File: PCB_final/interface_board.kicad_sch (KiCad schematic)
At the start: 106 parts, among them J1 02x30_Shift_Register_Connector, J2 02x30_ADC_Connector, U1 74HC595, U2 74HC595, U3 74HC595, U4 74HC595, U5 74HC595, U6 74HC595, U7 74HC595, U8 MAX11643EEG, U9 MAX11643EEG

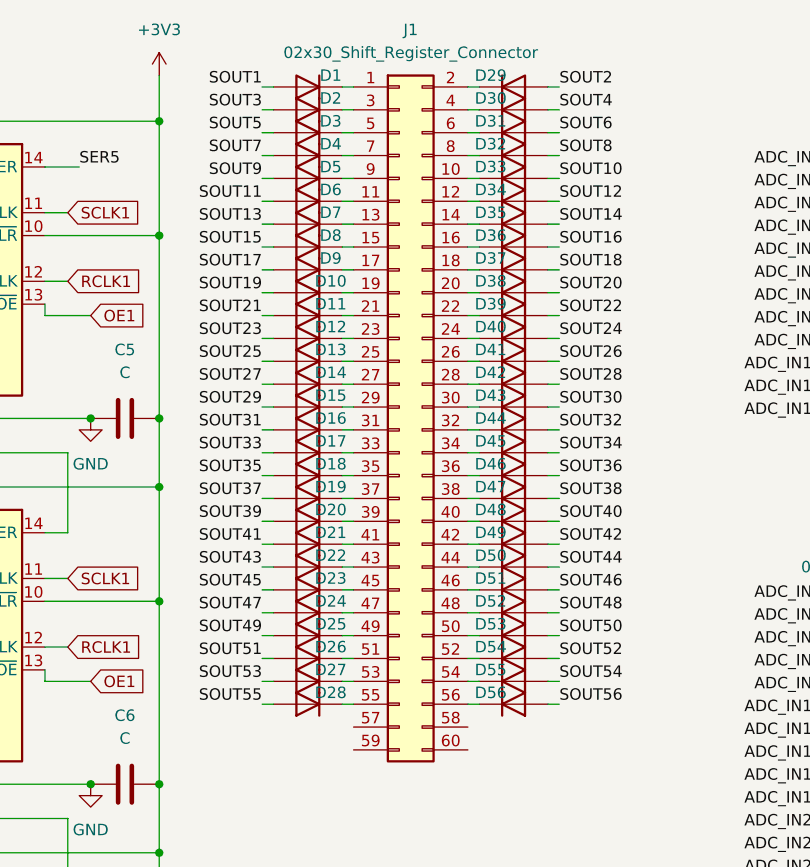
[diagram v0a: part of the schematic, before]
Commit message: changed diodes to the correct surface mount diodes we will be using on the final pcb
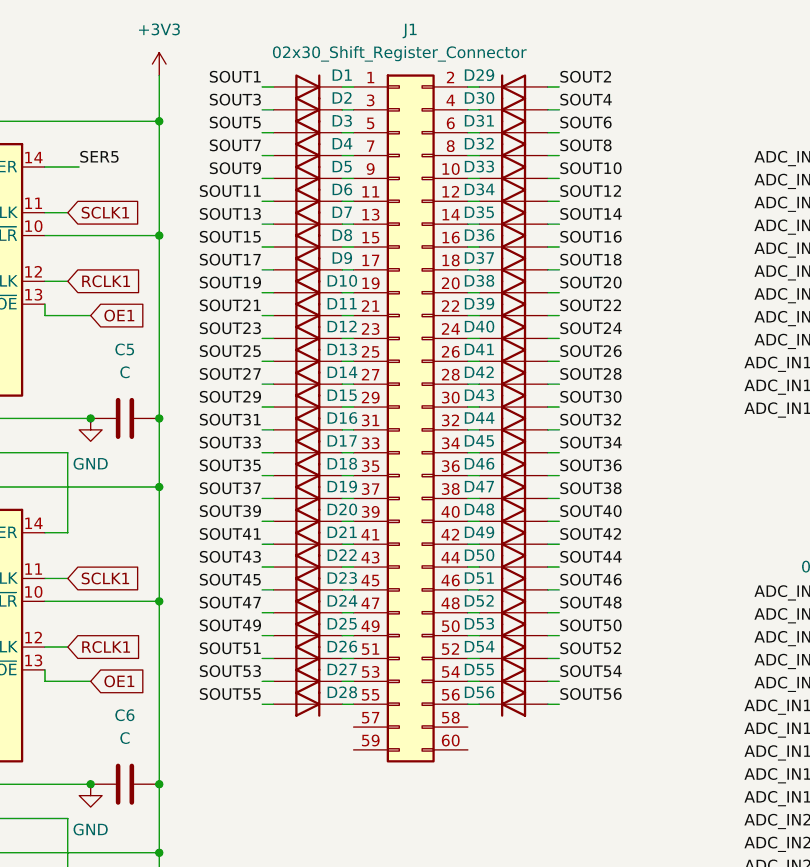
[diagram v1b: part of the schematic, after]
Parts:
- removed D1, D10, D11, D12, D13, D14, D15, D16, D17, D18, D19, D2, D20, D21, D22, D23, D24, D25, D26, D27, D28, D29, D3, D30, D31, D32, D33, D34, D35, D36, D37, D38, D39, D4, D40, D41, D42, D43, D44, D45, D46, D47, D48, D49, D5, D50, D51, D52, D53, D54, D55, D56, D6, D7, D8, D9: D, symbol Device:D
- added D1, D10, D11, D12, D13, D14, D15, D16, D17, D18, D19, D2, D20, D21, D22, D23, D24, D25, D26, D27, D28, D29, D3, D30, D31, D32, D33, D34, D35, D36, D37, D38, D39, D4, D40, D41, D42, D43, D44, D45, D46, D47, D48, D49, D5, D50, D51, D52, D53, D54, D55, D56, D6, D7, D8, D9: MMSD4148, Diode_SMD:D_SOD-123, symbol Diode:MMSD4148
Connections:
- net SOUT1: now also D1.2 (A)
- net SOUT10: now also D33.2 (A)
- net SOUT11: now also D6.2 (A)
- net SOUT12: now also D34.2 (A)
- net SOUT13: now also D7.2 (A)
- net SOUT14: now also D35.2 (A)
- net SOUT15: now also D8.2 (A)
- net SOUT16: now also D36.2 (A)
- net SOUT17: now also D9.2 (A)
- net SOUT18: now also D37.2 (A)
- net SOUT19: now also D10.2 (A)
- net SOUT2: now also D29.2 (A)
- net SOUT20: now also D38.2 (A)
- net SOUT21: now also D11.2 (A)
- net SOUT22: now also D39.2 (A)
- net SOUT23: now also D12.2 (A)
- net SOUT24: now also D40.2 (A)
- net SOUT25: now also D13.2 (A)
- net SOUT26: now also D41.2 (A)
- net SOUT27: now also D14.2 (A)
- net SOUT28: now also D42.2 (A)
- net SOUT29: now also D15.2 (A)
- net SOUT3: now also D2.2 (A)
- net SOUT30: now also D43.2 (A)
- net SOUT31: now also D16.2 (A)
- net SOUT32: now also D44.2 (A)
- net SOUT33: now also D17.2 (A)
- net SOUT34: now also D45.2 (A)
- net SOUT35: now also D18.2 (A)
- net SOUT36: now also D46.2 (A)
- net SOUT37: now also D19.2 (A)
- net SOUT38: now also D47.2 (A)
- net SOUT39: now also D20.2 (A)
- net SOUT4: now also D30.2 (A)
- net SOUT40: now also D48.2 (A)
- net SOUT41: now also D21.2 (A)
- net SOUT42: now also D49.2 (A)
- net SOUT43: now also D22.2 (A)
- net SOUT44: now also D50.2 (A)
- net SOUT45: now also D23.2 (A)
- net SOUT46: now also D51.2 (A)
- net SOUT47: now also D24.2 (A)
- net SOUT48: now also D52.2 (A)
- net SOUT49: now also D25.2 (A)
- net SOUT5: now also D3.2 (A)
- net SOUT50: now also D53.2 (A)
- net SOUT51: now also D26.2 (A)
- net SOUT52: now also D54.2 (A)
- net SOUT53: now also D27.2 (A)
- net SOUT54: now also D55.2 (A)
- net SOUT55: now also D28.2 (A)
- net SOUT56: now also D56.2 (A)
- net SOUT6: now also D31.2 (A)
- net SOUT7: now also D4.2 (A)
- net SOUT8: now also D32.2 (A)
- net SOUT9: now also D5.2 (A)
- net at J1.32 (Pin_32): now also D44.1 (K)
- net at J1.35 (Pin_35): now also D18.1 (K)
- net at J1.45 (Pin_45): now also D23.1 (K)
- net at J1.51 (Pin_51): now also D26.1 (K)
- net at J1.52 (Pin_52): now also D54.1 (K)
- net at J1.31 (Pin_31): now also D16.1 (K)
- net at J1.23 (Pin_23): now also D12.1 (K)
- net at J1.48 (Pin_48): now also D52.1 (K)
- net at J1.6 (Pin_6): now also D31.1 (K)
- net at J1.7 (Pin_7): now also D4.1 (K)
- net at J1.16 (Pin_16): now also D36.1 (K)
- net at J1.4 (Pin_4): now also D30.1 (K)
- net at J1.39 (Pin_39): now also D20.1 (K)
- net at J1.34 (Pin_34): now also D45.1 (K)
- net at J1.37 (Pin_37): now also D19.1 (K)
- net at J1.42 (Pin_42): now also D49.1 (K)
- net at J1.2 (Pin_2): now also D29.1 (K)
- net at J1.54 (Pin_54): now also D55.1 (K)
- net at J1.29 (Pin_29): now also D15.1 (K)
- net at J1.24 (Pin_24): now also D40.1 (K)
- net at J1.40 (Pin_40): now also D48.1 (K)
- net at J1.12 (Pin_12): now also D34.1 (K)
- net at J1.10 (Pin_10): now also D33.1 (K)
- net at J1.50 (Pin_50): now also D53.1 (K)
- net at J1.14 (Pin_14): now also D35.1 (K)
- net at J1.53 (Pin_53): now also D27.1 (K)
- net at J1.20 (Pin_20): now also D38.1 (K)
- net at J1.5 (Pin_5): now also D3.1 (K)
- net at J1.38 (Pin_38): now also D47.1 (K)
- net at J1.44 (Pin_44): now also D50.1 (K)
- net at J1.36 (Pin_36): now also D46.1 (K)
- net at J1.25 (Pin_25): now also D13.1 (K)
- net at J1.49 (Pin_49): now also D25.1 (K)
- net at J1.43 (Pin_43): now also D22.1 (K)
- net at J1.46 (Pin_46): now also D51.1 (K)
- net at J1.18 (Pin_18): now also D37.1 (K)
- net at J1.19 (Pin_19): now also D10.1 (K)
- net at J1.8 (Pin_8): now also D32.1 (K)
- net at J1.1 (Pin_1): now also D1.1 (K)
- net at J1.9 (Pin_9): now also D5.1 (K)
- net at J1.26 (Pin_26): now also D41.1 (K)
- net at J1.11 (Pin_11): now also D6.1 (K)
- net at J1.56 (Pin_56): now also D56.1 (K)
- net at J1.28 (Pin_28): now also D42.1 (K)
- net at J1.47 (Pin_47): now also D24.1 (K)
- net at J1.22 (Pin_22): now also D39.1 (K)
- net at J1.13 (Pin_13): now also D7.1 (K)
- net at J1.17 (Pin_17): now also D9.1 (K)
- net at J1.41 (Pin_41): now also D21.1 (K)
- net at J1.33 (Pin_33): now also D17.1 (K)
- net at J1.27 (Pin_27): now also D14.1 (K)
- net at J1.15 (Pin_15): now also D8.1 (K)
- net at J1.3 (Pin_3): now also D2.1 (K)
- net at J1.21 (Pin_21): now also D11.1 (K)
- net at J1.30 (Pin_30): now also D43.1 (K)
- net at J1.55 (Pin_55): now also D28.1 (K)

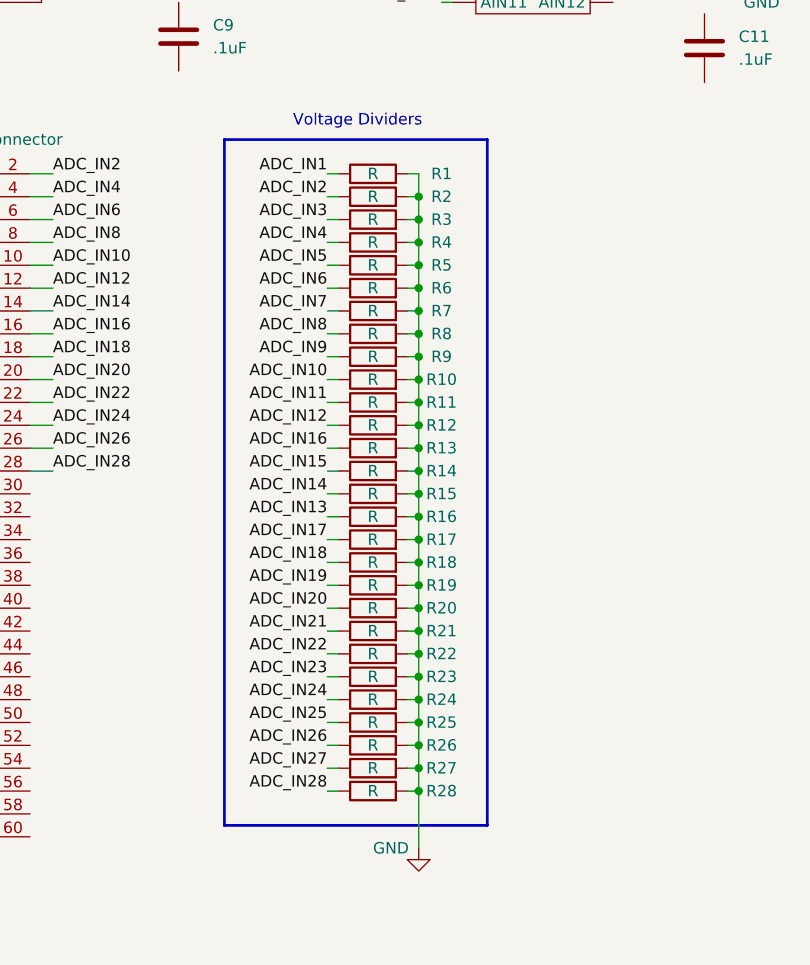
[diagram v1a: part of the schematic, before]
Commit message: changed all resistors to correct 100k value
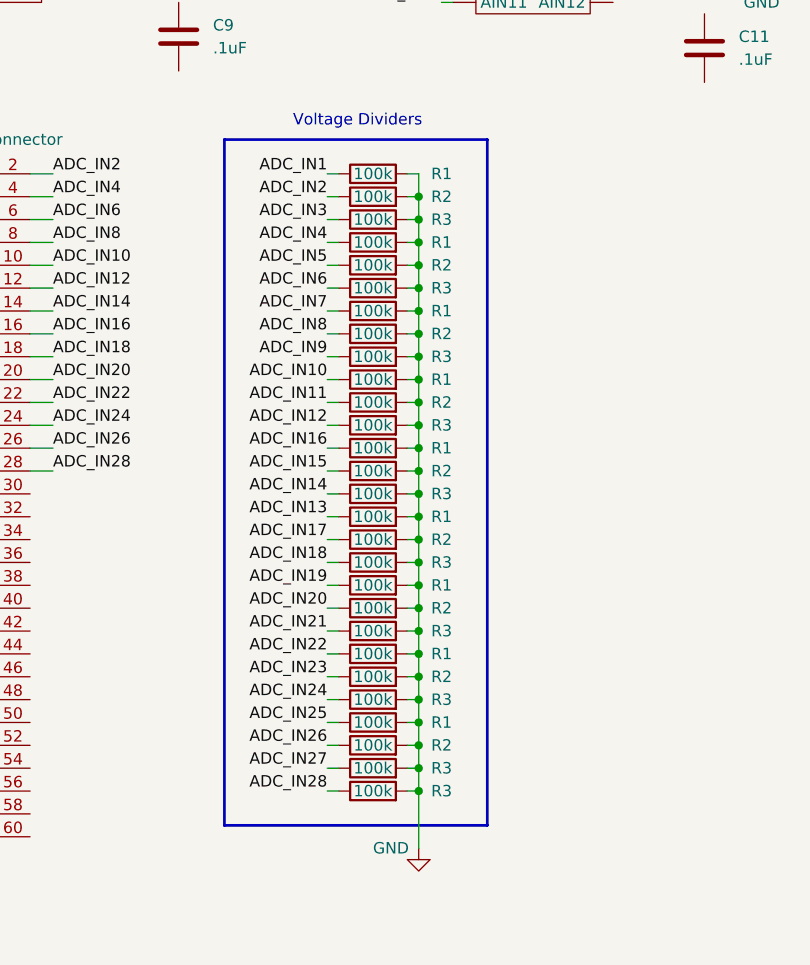
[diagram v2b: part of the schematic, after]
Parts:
- removed R10, R11, R12, R13, R14, R15, R16, R17, R18, R19, R20, R21, R22, R23, R24, R25, R26, R27, R28, R4, R5, R6, R7, R8, R9: R, symbol Device:R
- added R1 (x8), R2 (x8), R3 (x9): 100k, symbol Device:R
- R1, R2, R3: value R -> 100k
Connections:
- net ADC_IN10: now also R1.1
- net ADC_IN11: now also R2.1
- net ADC_IN12: now also R3.1
- net ADC_IN13: now also R1.1
- net ADC_IN14: now also R3.1
- net ADC_IN15: now also R2.1
- net ADC_IN16: now also R1.1
- net ADC_IN17: now also R2.1
- net ADC_IN18: now also R3.1
- net ADC_IN19: now also R1.1
- net ADC_IN20: now also R2.1
- net ADC_IN21: now also R3.1
- net ADC_IN22: now also R1.1
- net ADC_IN23: now also R2.1
- net ADC_IN24: now also R3.1
- net ADC_IN25: now also R1.1
- net ADC_IN26: now also R2.1
- net ADC_IN27: now also R3.1
- net ADC_IN28: now also R3.1
- net ADC_IN4: now also R1.1
- net ADC_IN5: now also R2.1
- net ADC_IN6: now also R3.1
- net ADC_IN7: now also R1.1
- net ADC_IN8: now also R2.1
- net ADC_IN9: now also R3.1
- net GND: now also R1.2, R1.2, R1.2, R1.2, R1.2, R1.2, R1.2, R1.2, R2.2, R2.2, R2.2, R2.2, R2.2, R2.2, R2.2, R2.2, R3.2, R3.2, R3.2, R3.2, R3.2, R3.2, R3.2, R3.2, R3.2

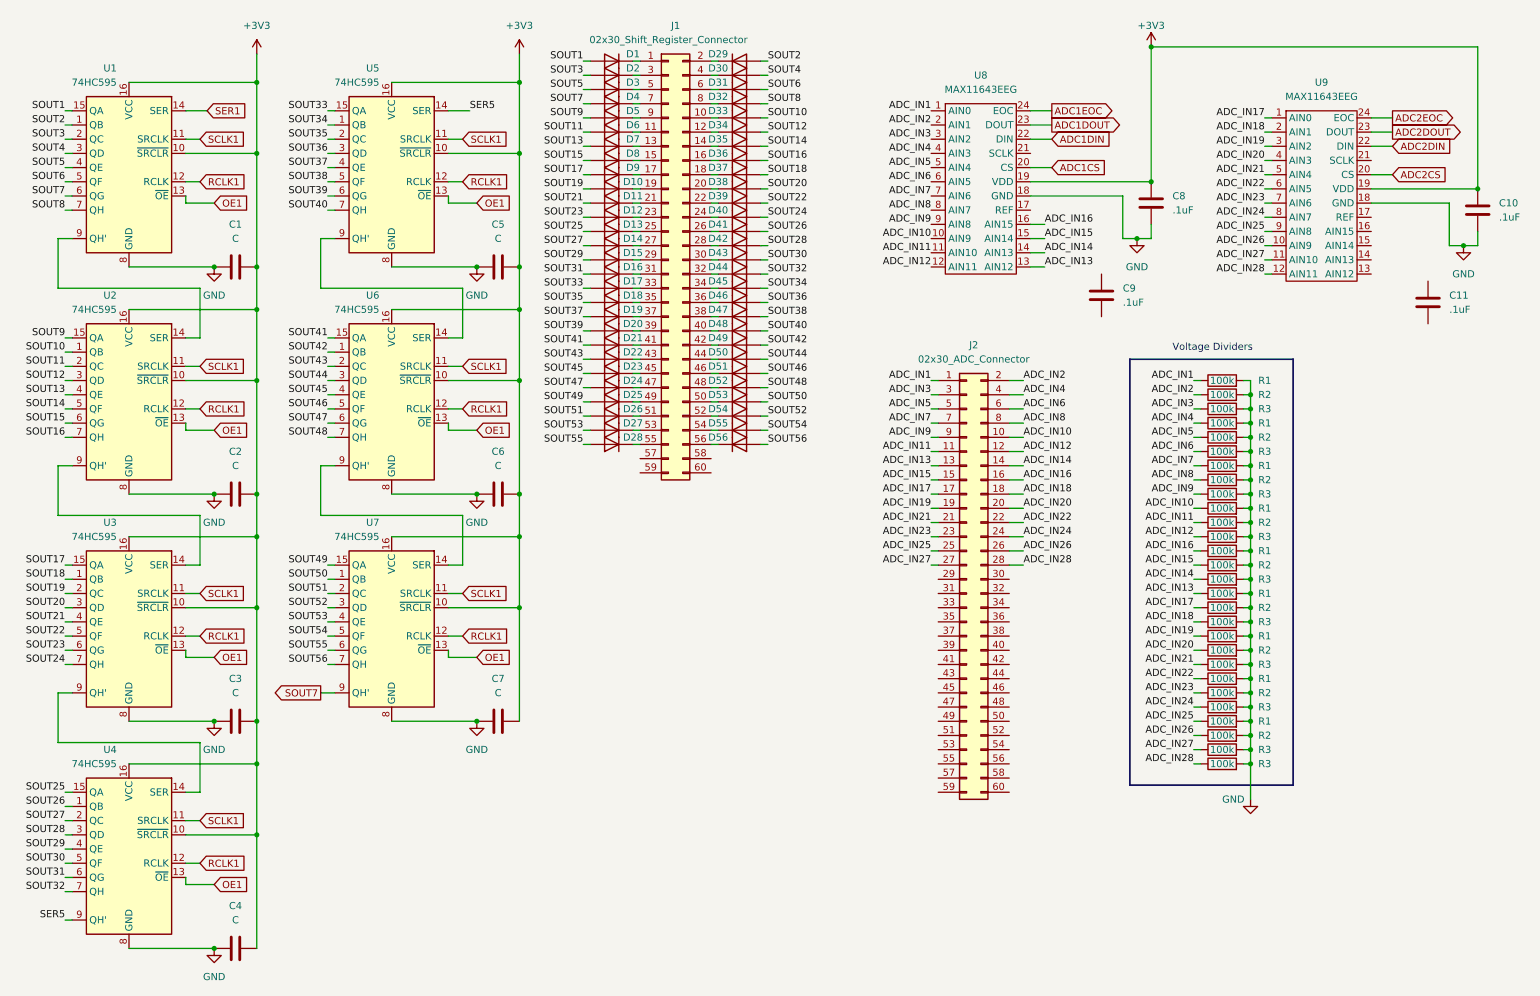
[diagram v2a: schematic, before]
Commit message: beautified shift registers by putting decoupling capacitors as external elements and put in actual capacitor values
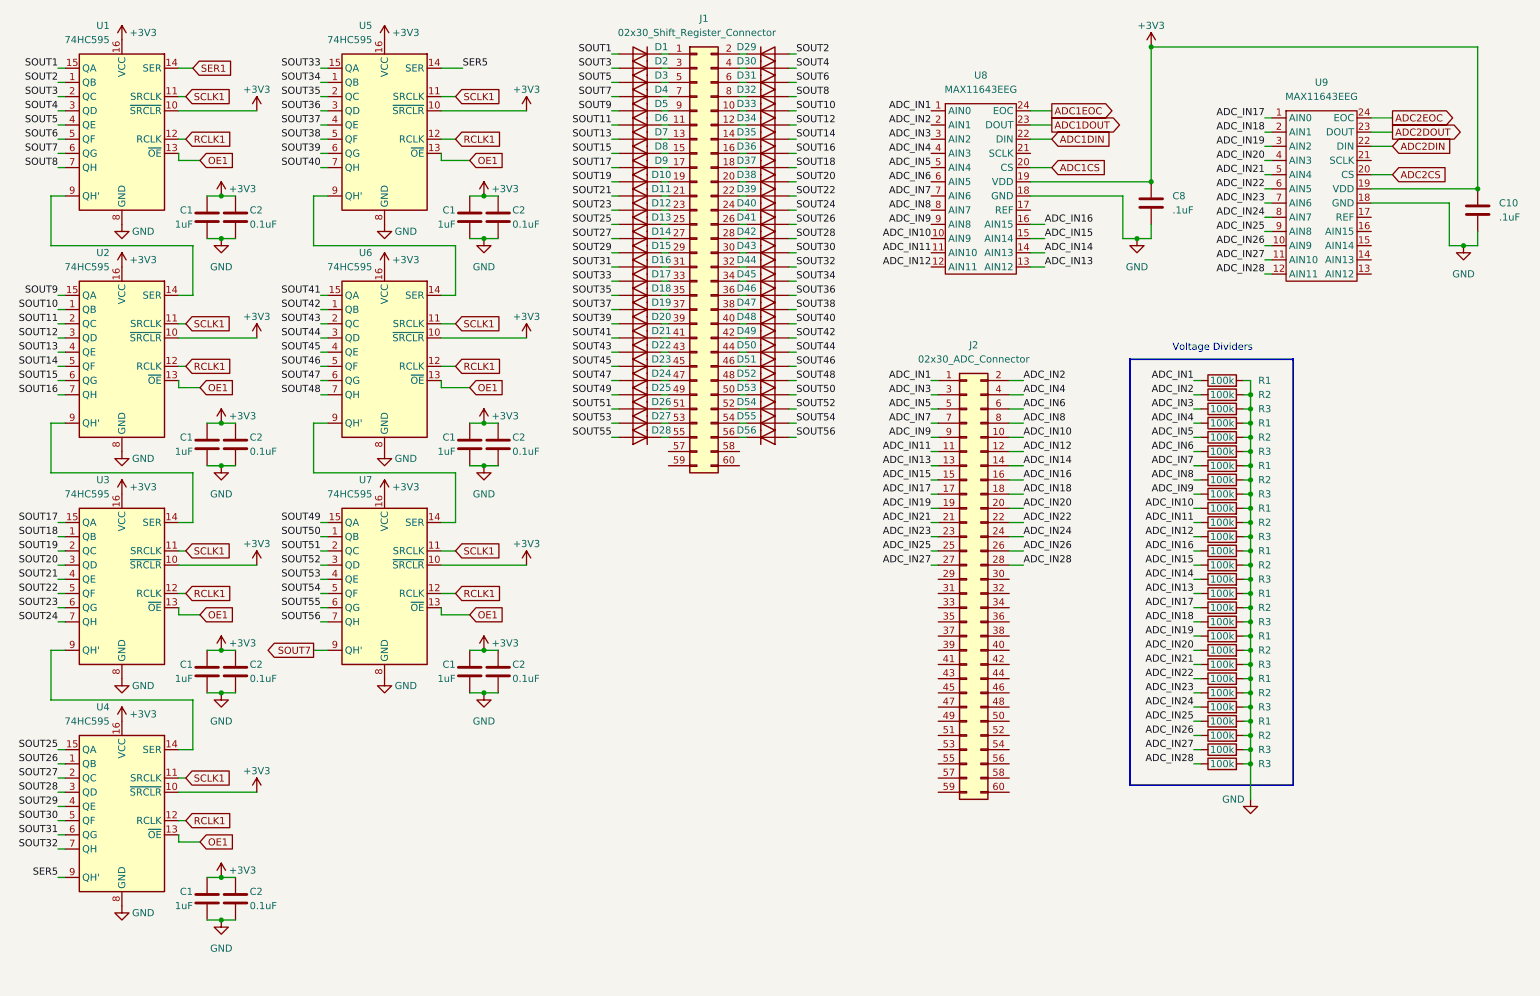
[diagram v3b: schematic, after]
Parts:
- removed C11, C9: .1uF, symbol Device:C
- removed C3, C4, C5, C6, C7: C, symbol Device:C
- added C1 (x6): 1uF, symbol Device:C
- added C2 (x6): 0.1uF, symbol Device:C
- C1: value C -> 1uF
- C2: value C -> 0.1uF
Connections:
- net +3V3: now also C1.1, C1.1, C1.1, C1.1, C1.1, C1.1, C2.1, C2.1, C2.1, C2.1, C2.1, C2.1
- net GND: now also C1.2, C1.2, C1.2, C1.2, C1.2, C1.2, C2.2, C2.2, C2.2, C2.2, C2.2, C2.2
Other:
- moved on the sheet: C1, C2, D1, D10, D11, D12, D13, D14, D15, D16, D17, D18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

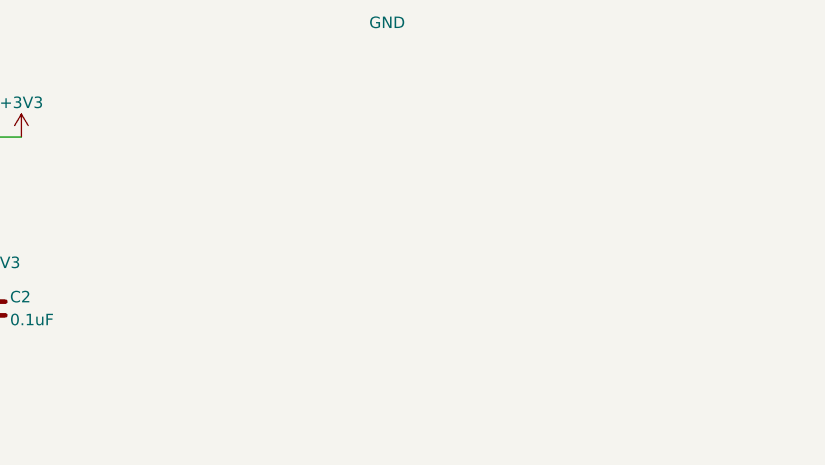
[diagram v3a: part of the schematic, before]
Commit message: Added active-low pass filter for power supply to schematic. Need to decide which OP AMP, resistor, and capacitor to use.
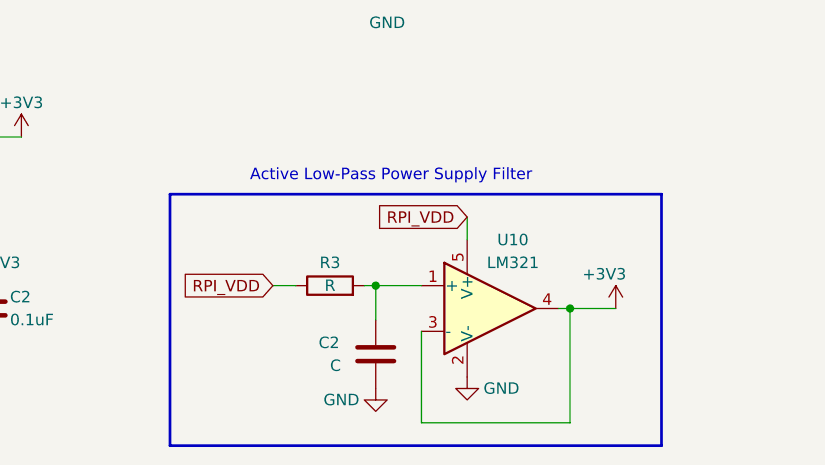
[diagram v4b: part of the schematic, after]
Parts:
- added C2: C, symbol Device:C
- added R3: R, symbol Device:R
- added U10: LM321, Package_TO_SOT_SMD:SOT-23-5, symbol Amplifier_Operational:LM321
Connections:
- net +3V3: now also U10.3 (-), U10.4
- net GND: now also C2.2, U10.2 (V-)
- new net: C2.1, R3.2, U10.1 (+)
- new net RPI_VDD: R3.1, U10.5 (V+)
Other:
- note added: "Active Low-Pass Power Supply Filter"
